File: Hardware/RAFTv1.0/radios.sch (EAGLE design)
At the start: 48 parts, among them U1 SX1276, X1 SMA-SMD, X2 SMA-SMD

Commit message: lora and gps schematics
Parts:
- removed C10, C21: (no value), rcl:C-US050-035X075
- removed C11, C12, C13, C14, C15, C16, C17, C18, C19, C20, C22, C23, C24, C25, C26, C27, C28, C29, C6, C7, C8, C9: (no value), rcl:C-US050-030X075
- removed C30, C31, C5: 100nF, rcl:C-US050-030X075
- removed L1, L2, L3, L4, L9: (no value), rcl:L-USL0201
- removed L10, L11, L12, L13, L5, L6, L7, L8: (no value), rcl:L-USL2012C
- removed QG1: TC49C, crystal:TC49C
- removed X1, X2: SMA-SMD, con-coax:SMA-SMD
- added C32, C33: 10nF, rcl:C-US050-030X075
- added C34, C35, C36, C37, C38, C40: 0.1uF, rcl:C-US050-030X075
- added C39: 0.1nF, rcl:C-US050-030X075
- added C41: 15pF, rcl:C-US050-030X075
- added C42: 0.75nF, rcl:C-US050-030X075
- added C43, C44: 0.47nF, rcl:C-USC0805
- added C45: 1.7pF, rcl:C-USC0805
- added C46, C47, C48, C49, C50: 100nF, rcl:C-USC0805
- added C51, C52: 15pF, rcl:C-USC0805
- added C53, C54, C66, C67, C75, C76: 47pF, rcl:C-USC0805
- added C55: 10nF, rcl:C-USC0805
- added C56: 47nF, rcl:C-USC0805
- added C57: 8.2pF, rcl:C-USC0805
- added C58: 22pF, rcl:C-USC0805
- added C59, C70, C71: 6.8pF, rcl:C-USC0805
- added C60: 3.3nH, rcl:C-USC0805
- added C61, C62, C63, C64, C69, C72, C74: (no value), rcl:C-USC0805
- added C65: 3.3pF, rcl:C-USC0805
- added C68, C77: 4.7pF, rcl:C-USC0805
- added C73: 2.7nH, rcl:C-USC0805
- added J1, J2: 132134-15, 132134-15:132134-15
- added L14, L18, L19: 5.6nH, rcl:L-USL3225M
- added L15: 33nH, rcl:L-USL3225M
- added L16: 1.5nH, rcl:L-USL3225M
- added L17: 82nH, rcl:L-USL3225M
- added L20: 0H, rcl:L-USL3225M
- added L21: (no value), rcl:L-USL3225M
- added L22, L26: 15nH, rcl:L-USL3225M
- added L23: 12nH, rcl:L-USL3225M
- added L24: 0R, rcl:L-USL3225M
- added L25: 18nH, rcl:L-USL3225M
- added Q1: (no value), special:XTAL/S
- added QG2: TC49C, crystal:TC49C
- added R1: 15k, rcl:R-US_R0805
- added R2, R3, R4: 0R, rcl:R-US_R0805
- added U2: MAX2771ETI+, MAX2771ETI_:MAX2771ETI+
- added U3: SX1276, SX1276:SX1276
- added U4, U5, U6: PE4259, PE4259:PE4259
- C1, C2: device rcl:C-US050-035X075 -> rcl:C-USC0805
- C3: value 100nF -> (none); device rcl:C-US050-030X075 -> rcl:C-USC0805; SPICEPREFIX 100nF -> (none)
- C4: value 100nF -> 1nF; device rcl:C-US050-030X075 -> rcl:C-USC0805
- U1: value SX1276 -> PE4259; device SX1276:SX1276 -> PE4259:PE4259
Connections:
- removed net N$10: C11.2, C13.2, L4.2, L5.1
- removed net N$21: C27.1, C28.2, L12.1
- removed net N$22: C29.2, L12.2, X2.1
- removed net N$23: C19.1, L8.1, U1.RFI_LF
- removed net N$9: C9.1, L4.1
- new net N$16: C33.2, QG2.VCC
- new net N$24: C32.2, QG2.OUT
- new net N$25: C32.1, U2.CLKOUT
- new net N$26: C33.1, U2.XTAL
- new net N$27: C41.1, R1.1, U2.CPOUT
- new net N$28: C42.1, R1.2
- new net N$29: L14.1, U2.LNAIN_HI
- new net N$30: C43.1, U2.LNAOUT_HI
- new net N$31: C44.2, C45.1, L14.2
- new net N$32: C43.2, U2.MIXIN_HI
- new net N$34: R2.1, U3.XTB
- new net N$35: C47.1, U3.VR_ANA
- new net N$36: C51.1, Q1.1, R2.2
- new net N$37: C49.1, U3.VR_DIG
- new net N$38: C52.1, Q1.2, U3.XTA
- new net N$39: C53.1, C54.1, C55.1, L15.1, L17.2, U3.VR_PA
- new net N$40: C68.2, C77.1, L17.1, U3.RFO_LF
- new net N$41: C57.2, C58.1, L15.2, L16.2
- new net N$42: L16.1, U3.PA_BOOST
- new net N$43: C58.2, L18.1
- new net N$44: C59.2, C62.1, L18.2, L19.1
- new net N$45: C60.2, C62.2, C63.2, L19.2, L20.1
- new net N$46: C61.2, C63.1, L20.2, U4.RF1
- new net N$47: C70.1, C73.1, L22.2, L23.1
- new net N$48: C64.2, L21.1, U3.RFI_HF(GND)
- new net N$49: C65.2, C66.1, L21.2
- new net N$50: C66.2, R3.1
- new net N$51: C67.1, R3.2
- new net N$52: C67.2, U4.RF2
- new net N$53: C77.2, L22.1
- new net N$54: C71.1, C73.2, C74.1
- new net N$55: L23.2, L24.1
- new net N$56: C72.1, C74.2, L24.2, U1.RF2
- new net N$57: L25.1, L26.1, U3.RFI_LF
- new net N$58: C69.1, C75.1, L26.2
- new net N$59: C75.2, R4.2
- new net N$60: C76.1, R4.1
- new net N$61: C76.2, U1.RF1
- new net N$90: U1.CTRL, U3.RXTX/RF_MOD, U4.CTRL
- new net VCC: C1.1, C2.1, C3.1, C4.1, C46.1, C48.1, C50.1, C56.1, U1.!CTRL/!VDD, U3.VBAT_ANA, U3.VBAT_DIG, U3.VBAT_RF, U4.!CTRL/!VDD, U5.!CTRL/!VDD, U6.!CTRL/!VDD
- net GND: now also C34.2, C35.2, C36.2, C37.2, C38.2, C39.2, C40.2, C41.2, C42.2, C45.2, C46.2, C47.2, C48.2, C49.2, C50.2, C51.2, C52.2, C53.2, C54.2, C55.2, C56.2, C57.1, C59.1, C60.1, C61.1, C64.1, C65.1, C68.1, C69.2, C70.2, C71.2, C72.2, L25.2, QG2.GND, QG2.GND1, U2.EP, U2.LNAIN_LO, U2.LNAOUT_LO, U2.MIXIN_LO, U3.EXP, U3.GND, U3.RFO_HF(GND), U4.GND, U5.GND, U6.GND; no longer C10.1, C13.1, C14.1, C15.1, C17.1, C18.1, C21.1, C24.1, C25.1, C26.1, C28.1, C29.1, C30.2, C31.2, C5.2, C6.2, C7.2, L3.2, QG1.GND, QG1.GND1, X1.2, X2.2
- net N$1: now also J1.SIG, U5.RFC; no longer C1.1, QG1.VCC, U1.XTB
- net N$11: now also U2.Q0; no longer C11.1, C12.2, C14.2, L5.2, L6.1
- net N$12: now also U2.Q1; no longer C12.1, C15.2, C16.2, L6.2
- net N$13: now also U2.I0; no longer C16.1, C17.2, L7.1
- net N$14: now also U2.I1; no longer C18.2, L7.2, X1.1
- net N$15: now also U2.SDATA; no longer C19.2, C20.2, C21.2, L13.2, U1.RFO_LF
- net N$17: now also U2.SCLK; no longer C20.1, L9.1
- net N$18: now also U2.CSN; no longer C22.2, C24.2, L10.1, L9.2
- net N$19: now also U2.SHDN; no longer C22.1, C23.2, C25.2, L10.2, L11.1
- net N$2: now also U4.RFC, U5.RF2; no longer C2.1, QG1.OUT, U1.XTA
- net N$20: now also U2.ADC_CLKIN; no longer C23.1, C26.2, C27.2, L11.2
- net N$3: now also U3.DIO5, U5.CTRL; no longer L13.1, L2.1, U1.PA_BOOST
- net N$4: now also U1.RFC, U5.RF1; no longer C5.1, U1.VR_DIG
- net N$5: now also C44.1, U6.RFC; no longer C4.1, U1.VR_ANA
- net N$6: now also U6.CTRL; no longer C6.1, C7.1, L1.1, U1.VR_PA
- net N$7: now also J2.SIG, U6.RF2; no longer C10.2, C8.1, C9.2, L1.2, L2.2
- net N$8: now also U6.RF1; no longer C8.2, L3.1, U1.RFI_HF(GND)
- net VDD: now also C34.1, C35.1, C36.1, C37.1, C38.1, C39.1, C40.1, U2.VCCADC, U2.VCCCP, U2.VCCD, U2.VCCIF, U2.VCCRF, U2.VCCVCO; no longer C3.1, C30.1, C31.1, U1.VBAT_ANA, U1.VBAT_DIG, U1.VBAT_RF

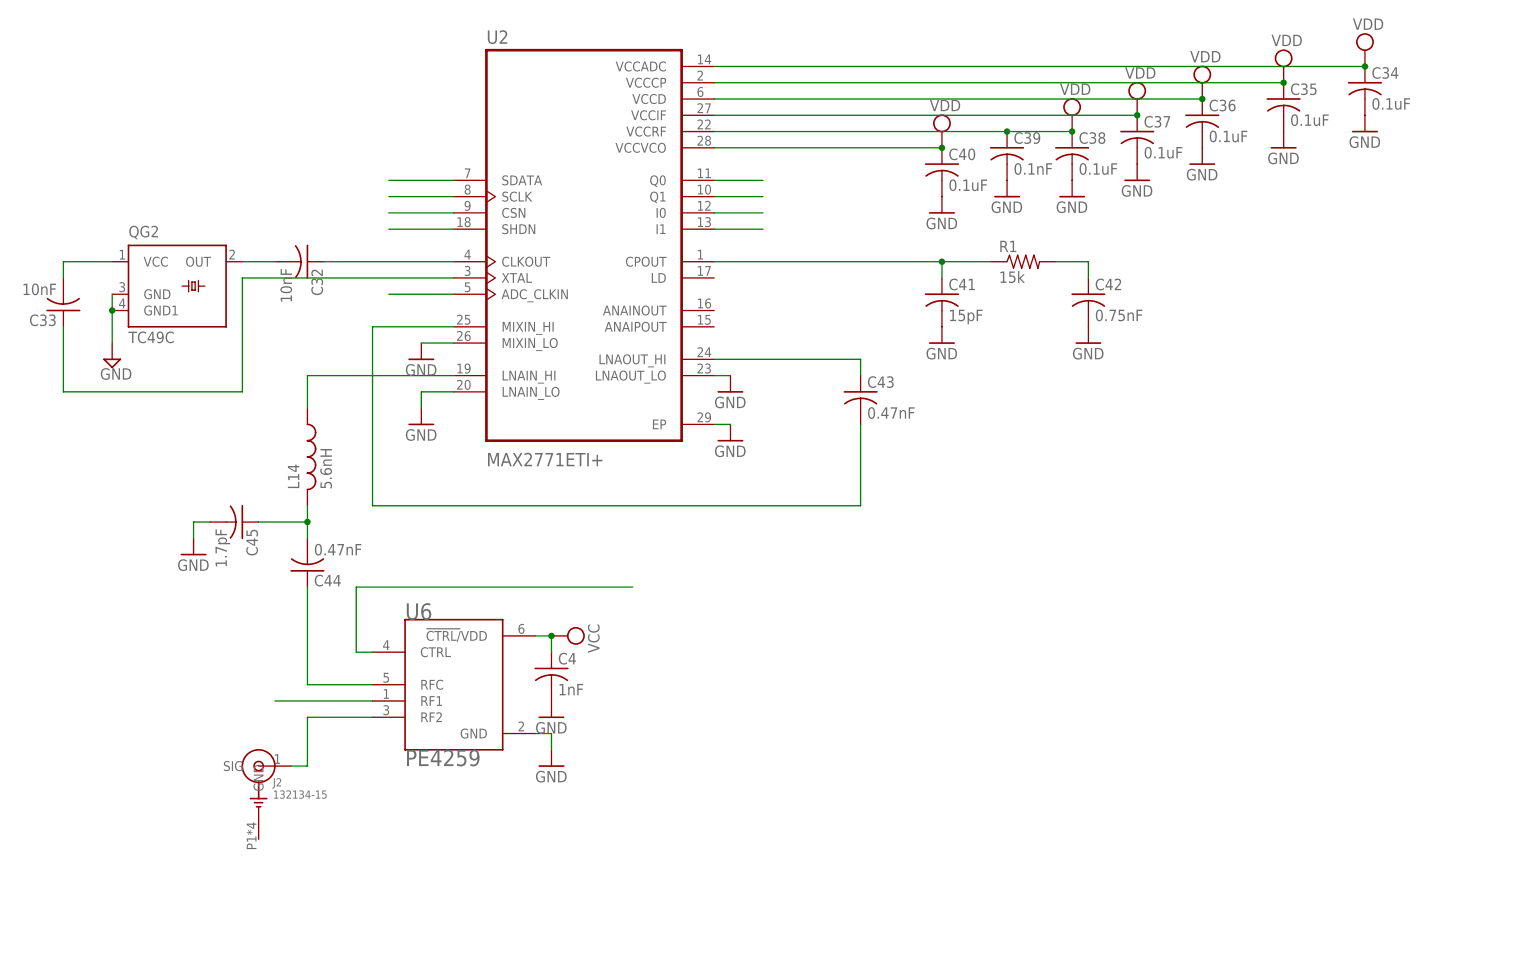
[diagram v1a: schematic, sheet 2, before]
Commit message: finalized gps. ref design for lora. renamed some libraries. added datasheets and started mcu schematic
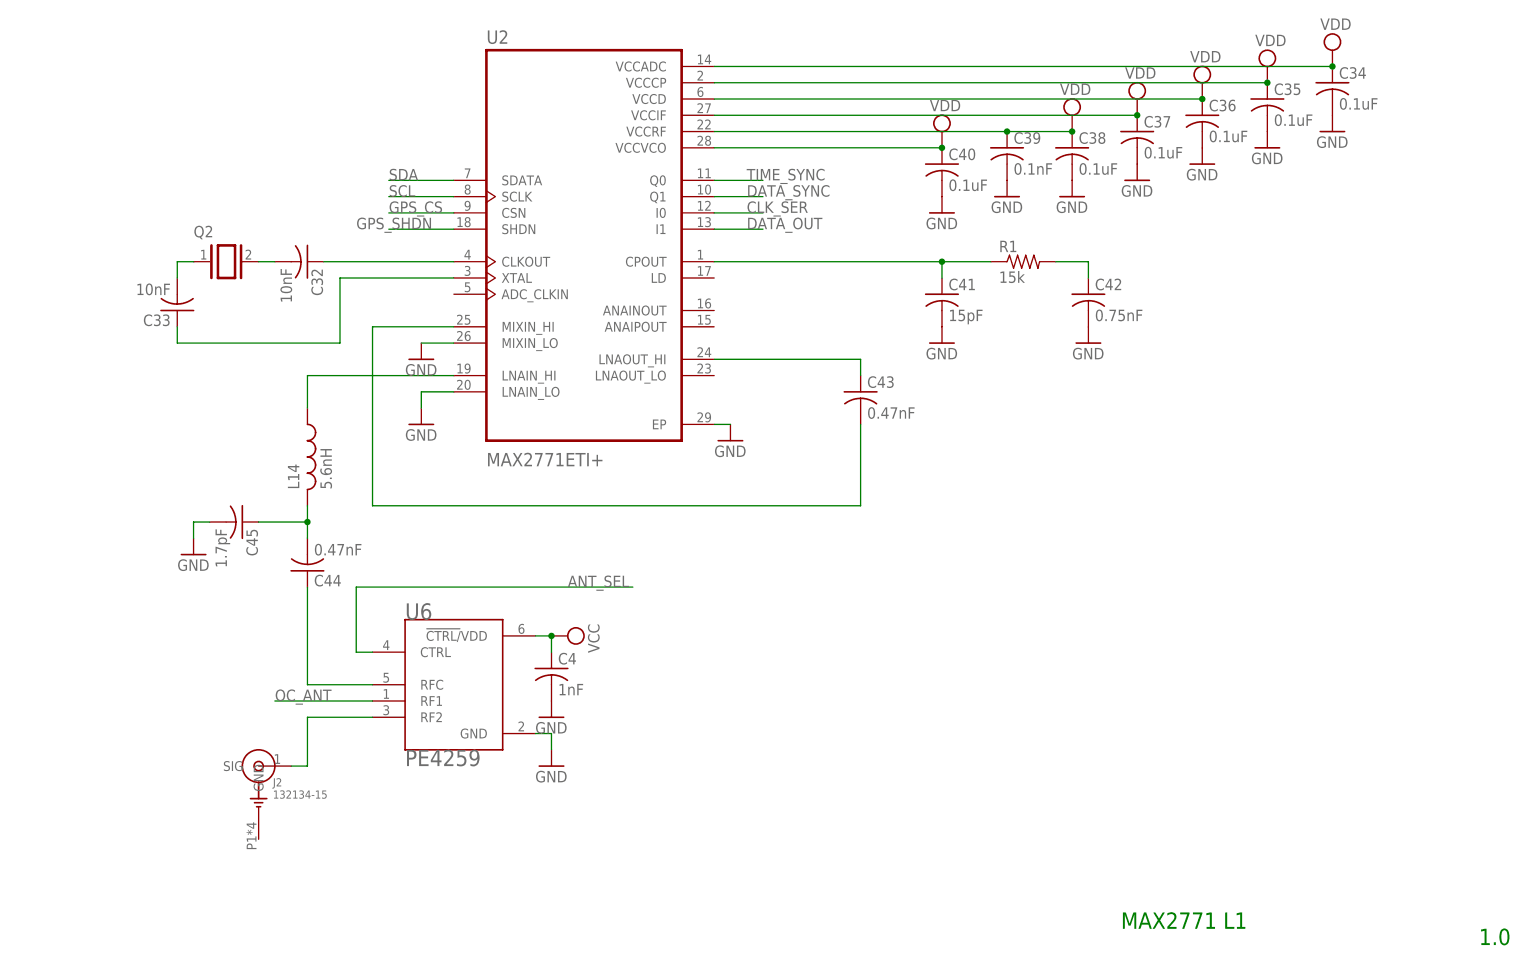
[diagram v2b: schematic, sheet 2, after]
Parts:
- removed QG2: TC49C, crystal:TC49C
- added Q2: (no value), special:XTAL/S
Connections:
- net N$11 renamed TIME_SYNC
- net N$12 renamed DATA_SYNC
- net N$13 renamed CLK_SER
- net N$14 renamed DATA_OUT
- net N$15 renamed SDA
- net N$17 renamed SCL
- net N$18 renamed GPS_CS
- net N$19 renamed GPS_SHDN
- net N$6 renamed ANT_SEL
- net N$8 renamed OC_ANT
- removed net N$16: C33.2, QG2.VCC
- removed net N$20: U2.ADC_CLKIN
- new net MISO: U3.MISO
- new net MOSI: U3.MOSI
- new net N$6: C33.2, Q2.1
- new net SPI_CLK: U3.SCK
- new net SX_CS: U3.NSS
- net GND: no longer QG2.GND, QG2.GND1, U2.LNAOUT_LO
- net N$24: now also Q2.2; no longer QG2.OUT
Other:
- note added: "1.0"
- note added: "1.2"
- note added: "MAX2771 L1"
- note added: "SX1276 RFH RFL - ref design"
- moved on the sheet: C33, C34, C35
